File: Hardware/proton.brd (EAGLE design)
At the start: 171.4 x 152.1 mm, 101 parts, among them IC1 MCP2300X/SO, IC2 MAX7219CWG, IC3 LD117AS33TR, J1 POWER_JACKPTH_LOCK, K1 ZF112, M2 WIRELESS-NRF24L01, P1 P120PK, Q1 BSS138, Q2 BSS138, SW1 ENCODER_SW1-PEC12, T1 BC847, T2 BC847, T3 BC847, U1 LCD-16X2SILK, U2 I2C EEPROM

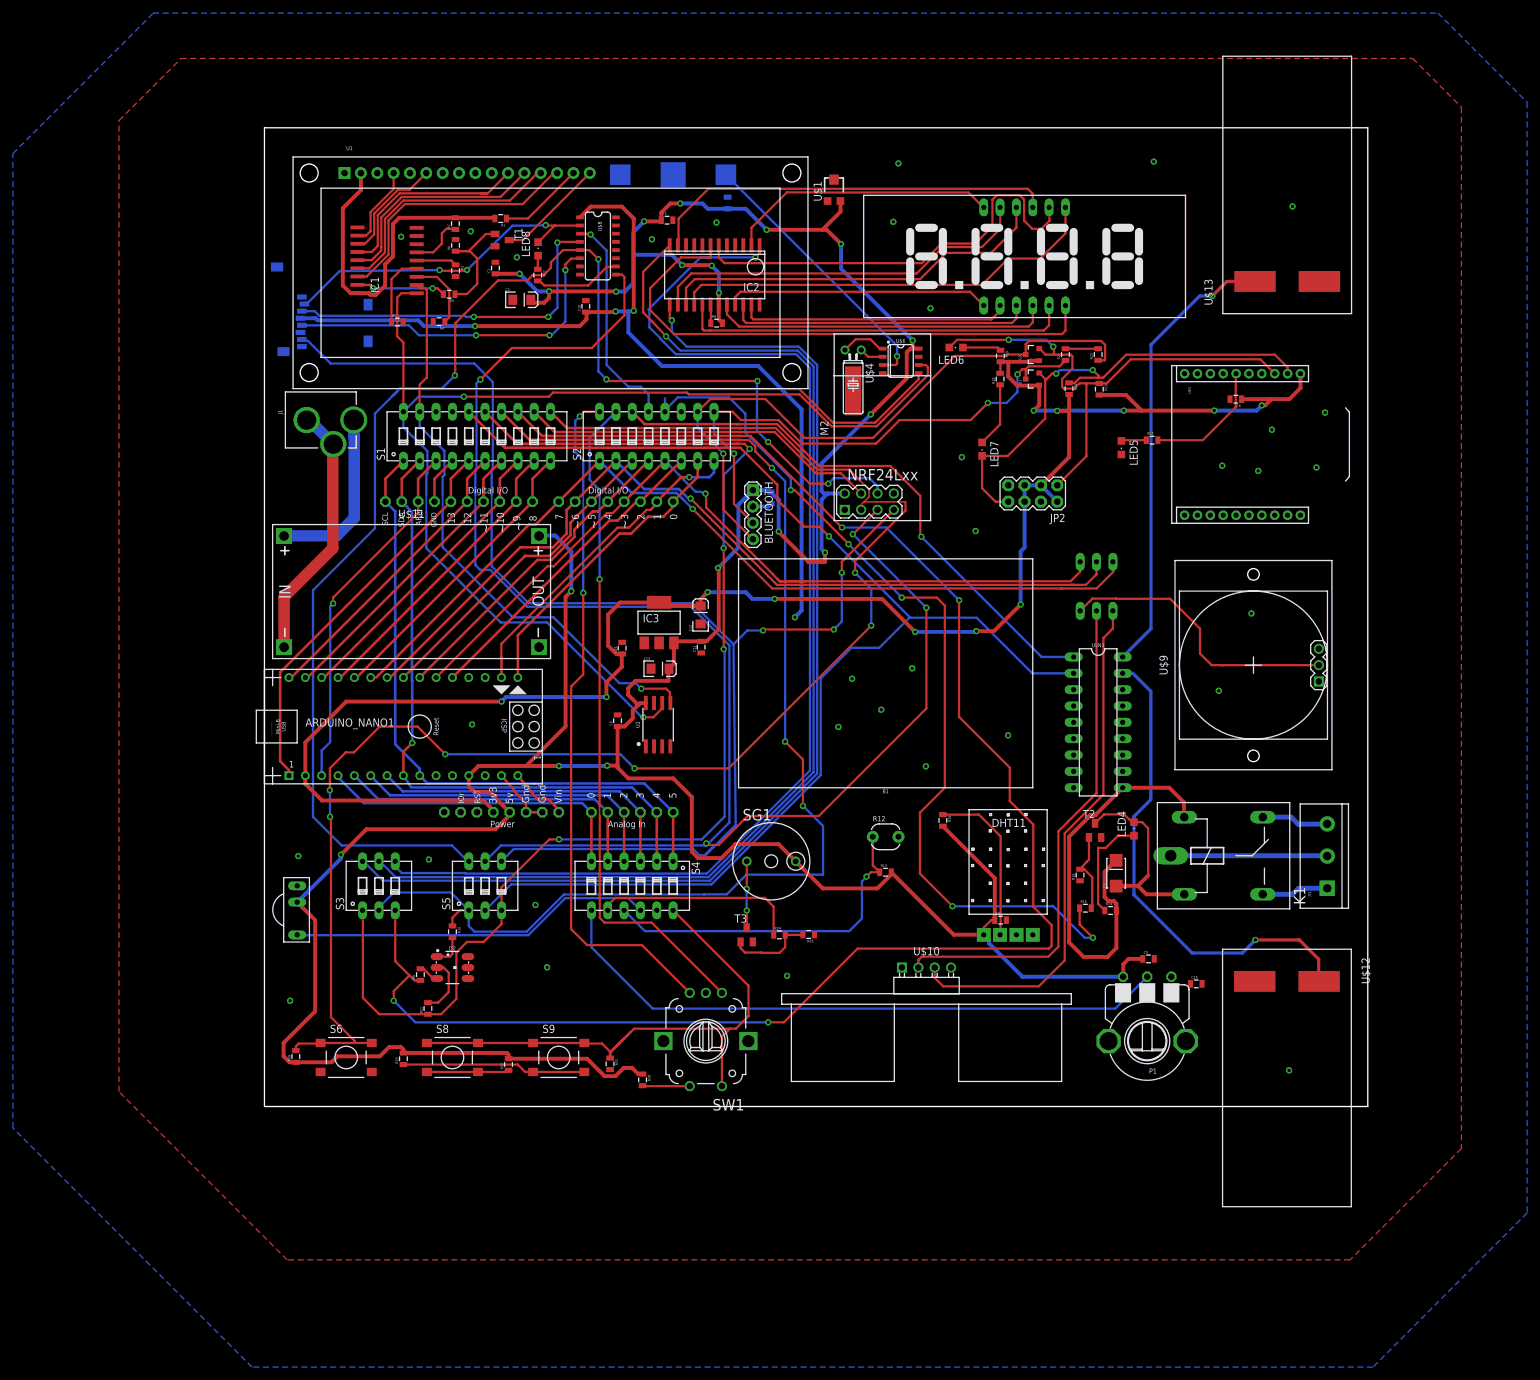
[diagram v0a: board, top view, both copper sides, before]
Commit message: Power rails and toggle switch
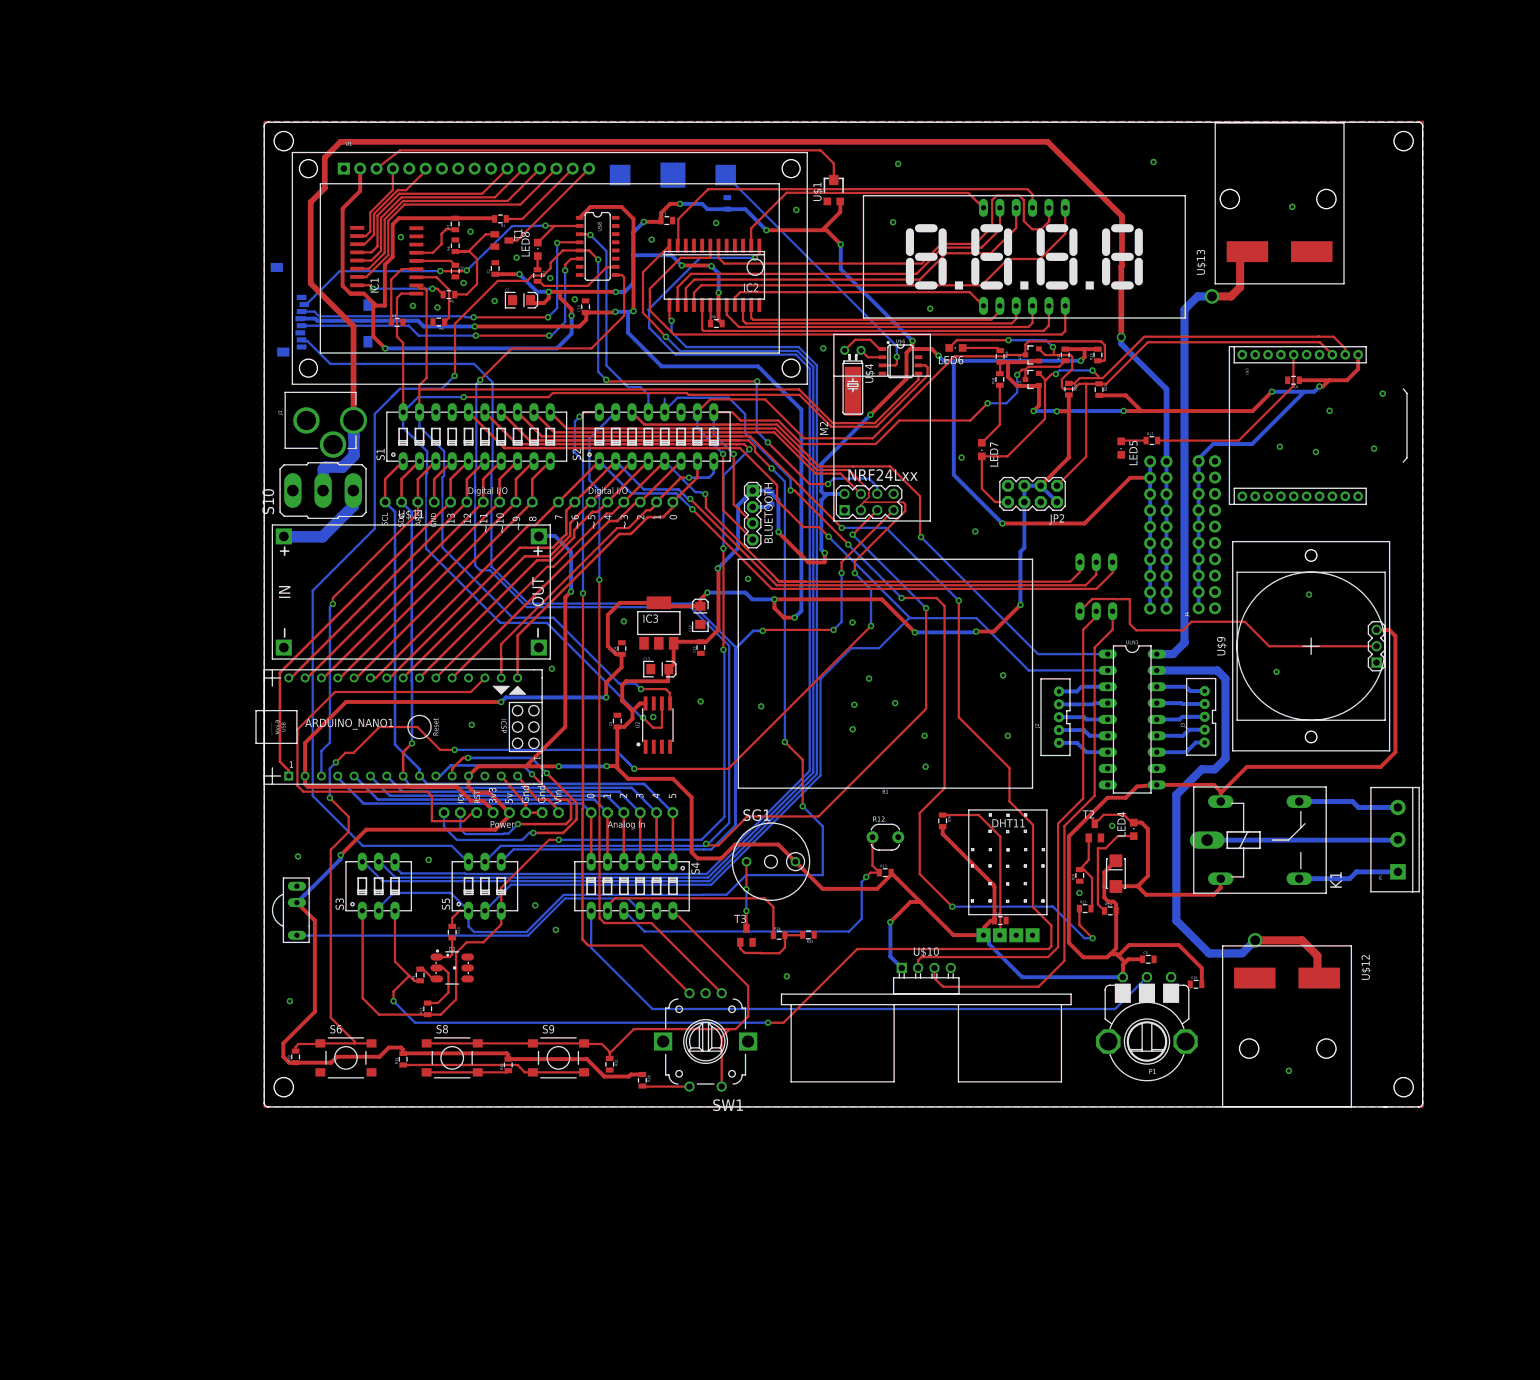
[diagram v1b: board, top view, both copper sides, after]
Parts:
- added J2, J3: (no value), SparkFun-Connectors:JST-5-PTH-VERT
- added J4, J5: (no value), SparkFun-Connectors:2X10_NOSILK
- added S10: (no value), switch:M9040P
- SW1: value ENCODER_SW1-PEC12 -> ENCODER
- moved JP1 11.3 mm to (176.1, 36.5)
- moved C6 9.43 mm to (159.9, 112.8)
- moved U$3 9.43 mm to (149.9, 105.8)
- moved U$9 9.43 mm to (162.6, 71.5)
- moved K1 6.16 mm to (154.7, 41.4)
- moved ULN1 5.31 mm to (134.8, 60.1)
- moved U$13 4.78 mm to (167.7, 127.8)
- moved U1 0.70 mm to (44.3, 130.2)
- moved U$12 0.52 mm to (148.9, 25.0)
- moved D1 0.07 mm to (132.3, 36.2)
- moved R22 0.07 mm to (129.7, 111.4)
- moved S7 0.07 mm to (129.2, 80.8)
- moved C15 0.07 mm to (144.7, 19.0)
- moved C5 0.07 mm to (137.3, 22.9)
- moved R14 0.07 mm to (131.4, 30.4)
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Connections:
- removed net 5V: U$10.1, U$9.3
- removed net N$2: J1.PWR, U$11.IN+
- new net +12V: J1.PWR, J5.10, J5.12, J5.14, J5.16, J5.18, J5.2, J5.20, J5.4, J5.6, J5.8, S10.2
- new net N$82: J3.5, ULN1.16
- new net N$83: J3.4, ULN1.15
- new net N$84: J3.3, ULN1.14
- new net N$85: J3.2, ULN1.13
- new net N$86: J3.1, ULN1.12
- new net N$87: J2.1, ULN1.7
- new net N$88: J2.2, ULN1.6
- new net N$89: J2.3, ULN1.5
- new net N$90: J2.4, ULN1.4
- new net N$91: J2.5, ULN1.3
- net +5V: now also J5.1, J5.11, J5.13, J5.15, J5.17, J5.19, J5.3, J5.5, J5.7, J5.9, U$10.1, U$9.3
- net 3.3V: now also J4.10, J4.12, J4.14, J4.16, J4.18, J4.2, J4.20, J4.4, J4.6, J4.8
- net GND: now also J1.GND, J1.GNDBREAK, J4.1, J4.11, J4.13, J4.15, J4.17, J4.19, J4.3, J4.5, J4.7, J4.9, U$11.IN-
- net N$3: now also S10.3, U$11.IN+; no longer J1.GND, J1.GNDBREAK, U$11.IN-
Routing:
- net +12V: track 0.00 -> 252.6 mm, vias 0 -> 1
- net +5V: track 724.4 -> 952.8 mm, vias 19 -> 25
- net N$34: track 0.00 -> 75.4 mm
- net RST: track 0.00 -> 74.1 mm
- net 3.3V: track 439.8 -> 501.9 mm
- net -A7: track 0.00 -> 51.6 mm, vias 0 -> 3
- net -A6: track 0.00 -> 47.6 mm, vias 0 -> 2
- net N$2: track 27.3 -> 0.00 mm
- net MISO: track 212.1 -> 239.4 mm
- net N$3: track 40.4 -> 15.2 mm
- net DOUT: track 76.8 -> 86.9 mm
- net RSSI: track 19.5 -> 29.5 mm
- net DIN: track 83.1 -> 93.1 mm
- net A5: track 94.0 -> 84.6 mm
- net _D3: track 44.8 -> 53.3 mm
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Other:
- board size 171.4 x 152.1 mm -> 180 x 153 mm

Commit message: properly sorted the pin-distributions, changed the motor drievr
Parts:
- removed J4, J5: (no value), SparkFun-Connectors:2X10_NOSILK
- removed LED8: Blue, led:CHIPLED_0805
- removed S6, S8, S9: DTSM-6, switch-tact:DTSM-6
- removed ULN1: (no value), SparkFun-IC-Special-Function:DIL18
- added C16: 100nf, SparkFun:0805
- added C17, C18, C19, C20: .1ufF, SparkFun:0805
- added IC4: L293D, st-microelectronics:DIL16
- added LED1: Yellow, led:CHIPLED_0805
- added S11: (no value), switch-dil:DIP10YL
- added S12: (no value), switch-dil:DIP08YL
- added S14: (no value), switch-dil:DIP06YL
- added T/H: (no value), DHT11:DHT11
- J2, J3: device SparkFun-Connectors:JST-5-PTH-VERT -> SparkFun-Connectors:2X5_NOSILK
- S1: value (none) -> DTSM-6; device switch-dil:DIP10YL -> switch-tact:DTSM-6
- S2: value (none) -> DTSM-6; device switch-dil:DIP08YL -> switch-tact:DTSM-6
- S3: value (none) -> DTSM-6; device switch-dil:DIP03YL -> switch-tact:DTSM-6
- S4: device switch-dil:DIP06YL -> switch-dil:DIP05YL
- U$7: device DHT11:DHT11 -> SparkFun-Aesthetics:OSHW-LOGO-L
- moved S2 101.6 mm to (29.2, 7.56)
- moved U$7 101.5 mm to (15.6, 20.1)
- moved S1 98.6 mm to (12.7, 7.56)
- moved C7 39.1 mm to (104.5, 118.7), flipped to the top, turned to 0 degrees
- moved S3 38.6 mm to (45.7, 7.56)
- moved S4 36.7 mm to (20.4, 34.0)
- moved J2 29.4 mm to (147.7, 77.3)
- moved C2 24.8 mm to (15.6, 120.5)
- moved C1 21.1 mm to (16.0, 123.0), turned to 180 degrees
- moved J3 18.9 mm to (137.6, 77.3), flipped to the bottom
- moved C10 15.5 mm to (48.1, 139.7), turned to 180 degrees
- moved R11 13.5 mm to (31.8, 27.1), turned to 270 degrees
- moved C5 11.4 mm to (131.4, 32.6), turned to 180 degrees
- moved R9 6.92 mm to (26.1, 27.1), turned to 270 degrees
- moved C9 5.93 mm to (108.4, 28.7), turned to 180 degrees
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- renumbered SG1 to BUZZER
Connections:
- removed net N$82: J3.5, ULN1.16
- removed net N$83: J3.4, ULN1.15
- removed net N$84: J3.3, ULN1.14
- removed net N$85: J3.2, ULN1.13
- removed net N$86: J3.1, ULN1.12
- removed net N$87: J2.1, ULN1.7
- removed net N$88: J2.2, ULN1.6
- removed net N$89: J2.3, ULN1.5
- removed net N$90: J2.4, ULN1.4
- removed net N$91: J2.5, ULN1.3
- new net A6: P1.S, S4.7
- new net A7: R12.1, R13.1, S4.6
- new net N$9: C18.2, IC4.11, U$13.P$2
- net +12V: now also J3.10, J3.2, J3.4, J3.6, J3.8; no longer J5.10, J5.12, J5.14, J5.16, J5.18, J5.2, J5.20, J5.4, J5.6, J5.8
- net +5V: now also C16.1, IC4.1, IC4.16, IC4.8, IC4.9, J3.1, J3.3, J3.5, J3.7, J3.9, T/H.VCC; no longer J5.1, J5.11, J5.13, J5.15, J5.17, J5.19, J5.3, J5.5, J5.7, J5.9, U$7.VCC, ULN1.10
- net -A0: now also S14.6; no longer S4.6
- net -A1: now also S14.5; no longer S4.5
- net -A2: now also S14.4; no longer S4.4
- net -A3: now also S14.3; no longer S4.3
- net -A6: now also S4.4
- net -A7: now also S4.5
- net -AREF: now also S11.3; no longer S1.3
- net -D10: now also S11.8; no longer S1.8
- net -D11: now also M2.6, S11.7, S5.1; no longer S1.7
- net -D12: now also M2.7, S11.6, S5.3; no longer S1.6
- net -D13: now also M2.5, S11.5, S5.2; no longer S1.5
- net -D2: now also S12.6; no longer S2.6
- net -D3: now also S12.5; no longer S2.5
- net -D4: now also S12.4; no longer S2.4
- net -D5: now also S12.3; no longer S2.3
- net -D6: now also S12.2; no longer S2.2
- net -D7: now also S12.1; no longer S2.1
- net -D8: now also S11.10; no longer S1.10
- net -D9: now also S11.9; no longer S1.9
- net -RX: now also S12.8; no longer S2.8
- net -SCL: now also S11.1, S14.1; no longer S1.1, S4.1
- net -SDA: now also S11.2, S14.2; no longer S1.2, S4.2
- net -TX: now also S12.7; no longer S2.7
- net 3.3V: now also J2.10, J2.2, J2.4, J2.6, J2.8; no longer J4.10, J4.12, J4.14, J4.16, J4.18, J4.2, J4.20, J4.4, J4.6, J4.8
- net A0: now also IC4.2, S14.7; no longer P1.S, S4.7
- net A1: now also R31.1, S14.8, S2.1, S2.2, S3.1, S3.2, SW1.P1; no longer R24.1, S4.8
- net A2: now also R26.1, S14.9, T/H.DATA; no longer R12.1, R13.1, S4.9
- net A3: now also S14.10; no longer S4.10
- net A4: now also S14.11; no longer S4.11
- net A5: now also S14.12; no longer R31.1, S4.12, S8.1, S8.2, S9.1, S9.2, SW1.P1
- net AREF: now also S11.18; no longer S1.18
- net D10: now also S11.13, S4.3; no longer S1.13, S3.3
- net D11: now also S11.14, S4.2; no longer S1.14, S3.2, S5.1
- net D12: now also S11.15, S4.1; no longer S1.15, S3.1, S5.3
- net D13: now also S11.16; no longer S1.16, S5.2, ULN1.2
- net D2: now also R24.1, S12.11; no longer S2.11
- net D3: now also S12.12; no longer S2.12
- net D4: now also S12.13; no longer S2.13
- net D5: now also IC4.15, S12.14; no longer S2.14, ULN1.1
- net D6: now also S12.15; no longer S2.15
- net D7: now also S12.16; no longer S2.16
- net D8: now also S1.1, S1.2, S11.11; no longer S1.11, S6.1, S6.2
- net D9: now also S11.12; no longer S1.12
- net GND: now also C16.2, C17.1, C18.1, C19.1, C20.1, IC4.10, IC4.12, IC4.13, IC4.4, IC4.5, IC4.7, J2.1, J2.3, J2.5, J2.7, J2.9, S1.3, S11.17, S11.4, T/H.GND; no longer J4.1, J4.11, J4.13, J4.15, J4.17, J4.19, J4.3, J4.5, J4.7, J4.9, S1.17, S6.3, S6.4, U$12.P$2, U$13.P$2, U$7.GND, ULN1.9
- net MISO: no longer M2.7
- net MOSI: no longer M2.6
- net MOTOR1: now also C17.2, IC4.14; no longer ULN1.18
- net MOTOR2: now also C20.2, IC4.3; no longer ULN1.17
- net N$1: now also C19.2, IC4.6, U$12.P$2; no longer R26.1, U$7.DATA
- net N$11: now also S3.3, S3.4; no longer S9.3, S9.4
- net N$42: now also LED1.A; no longer LED8.A
- net N$43: now also LED1.C; no longer LED8.C
- net N$5: now also S2.3, S2.4; no longer S8.3, S8.4
- net RX: now also S12.9; no longer S2.9
- net SCK: no longer M2.5
- net SCL: now also S11.20; no longer S1.20
- net SDA: now also S11.19; no longer S1.19
- net S_D10: now also S4.8; no longer S3.4
- net S_D11: now also S4.9; no longer S3.5
- net S_D12: now also S4.10; no longer S3.6
- net TX: now also S12.10; no longer S2.10
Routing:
- net D13: track 211.1 -> 0.00 mm, vias 1 -> 0
- net -D13: track 61.6 -> 224.3 mm, vias 0 -> 4
- net -D12: track 46.5 -> 207.4 mm, vias 0 -> 3
- net -D11: track 46.5 -> 204.1 mm, vias 0 -> 3
- net A6: track 0.00 -> 134.4 mm, vias 0 -> 2
- net A7: track 0.00 -> 112.9 mm, vias 0 -> 2
- net D2: track 0.00 -> 107.7 mm, vias 0 -> 7
- net N$9: track 0.00 -> 107.3 mm, vias 0 -> 1
- net A5: track 84.6 -> 0.00 mm
- net A0: track 98.1 -> 169.9 mm
- net MOSI: track 218.6 -> 160.6 mm, vias 6 -> 2
- net A1: track 32.0 -> 77.9 mm, vias 0 -> 1
- net A2: track 54.2 -> 99.2 mm
- net D10: track 266.9 -> 222.3 mm, vias 4 -> 6
- net SCK: track 256.0 -> 213.4 mm, vias 4 -> 2
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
